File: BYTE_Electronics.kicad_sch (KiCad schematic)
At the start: 9 parts, among them J3 Screw_Terminal_01x04, J4 Screw_Terminal_01x02, J7 Screw_Terminal_01x02, J9 Screw_Terminal_01x02, U1 LM2596S-3.3

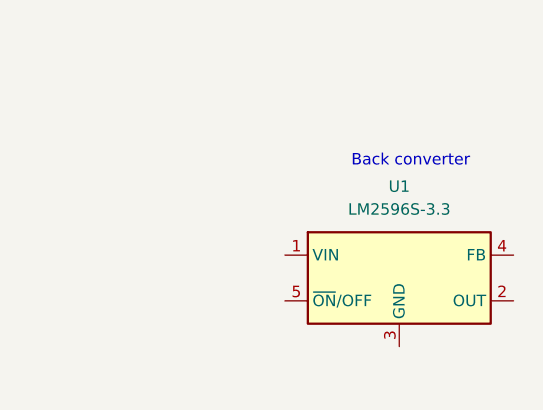
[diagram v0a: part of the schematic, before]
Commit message: Footprint added and minor changes
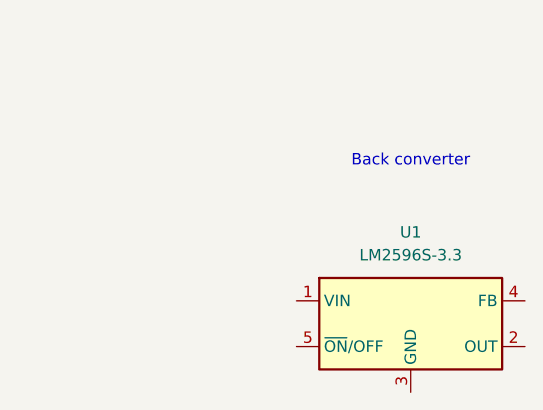
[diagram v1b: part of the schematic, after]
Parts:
- J9: footprint (none) -> Connector_AMASS:AMASS_XT60IPW-M_1x03_P7.20mm_Horizontal; LCSC (none) -> C5334533
- U1: footprint Package_TO_SOT_SMD:TO-263-5_TabPin3 -> Library_mis componentes:BEC_Matek_12S_Pro
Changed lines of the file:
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@@
 			)
 		)
-		(property "Footprint" ""
+		(property "Footprint" "Connector_AMASS:AMASS_XT60IPW-M_1x03_P7.20mm_Horizontal"
 			(at 113.03 27.94 0)
 			(effects
@@
 			)
 		)
+		(property "LCSC" "C5334533"
+			(at 113.03 27.94 0)
+			(effects
+				(font
+					(size 1.27 1.27)
+				)
+				(hide yes)
+			)
+		)
 		(pin "1"
 		)
@@
 				(path "/0c60501e-60f9-4c7f-923a-18a46703e785"
 					(reference "J9")
+					(unit 1)
+				)
+			)
+		)
+	)
+	(symbol
+		(lib_id "Regulator_Switching:LM2596S-3.3")
+		(at 133.35 119.38 0)
+		(unit 1)
+		(exclude_from_sim no)
+		(in_bom yes)
+		(on_board yes)
+		(dnp no)
+		(fields_autoplaced yes)
+		(property "Reference" "U1"
+			(at 133.35 109.22 0)
+			(effects
+				(font
+					(size 1.27 1.27)
+				)
+			)
+		)
+		(property "Value" "LM2596S-3.3"
+			(at 133.35 111.76 0)
+			(effects
+				(font
+					(size 1.27 1.27)
+				)
+			)
+		)
+		(property "Footprint" "Library_mis componentes:BEC_Matek_12S_Pro"
+			(at 134.62 125.73 0)
+			(effects
+				(font
+					(size 1.27 1.27)
+					(italic yes)
+				)
+				(justify left)
+				(hide yes)
+			)
+		)
+		(property "Datasheet" ""
+			(at 133.35 119.38 0)
+			(effects
+				(font
+					(size 1.27 1.27)
+				)
+				(hide yes)
+			)
+		)
+		(property "Description" ""
+			(at 133.35 119.38 0)
+			(effects
+				(font
+					(size 1.27 1.27)
+				)
+				(hide yes)
+			)
+		)
+		(pin "4"
+		)
+		(pin "1"
+		)
+		(pin "3"
+		)
+		(pin "2"
+		)
+		(pin "5"
+		)
+		(instances
+			(project ""
+				(path "/0c60501e-60f9-4c7f-923a-18a46703e785"
+					(reference "U1")
 					(unit 1)
 				)
@@
 			)
 		)
+		(property "LCSC" ""
+			(at 52.07 113.03 0)
+			(effects
+				(font
+					(size 1.27 1.27)
+				)
+				(hide yes)
+			)
+		)
 		(pin "1"
 		)
@@
 			)
 		)
+		(property "LCSC" ""
+			(at 113.03 46.99 0)
+			(effects
+				(font
+					(size 1.27 1.27)
+				)
+				(hide yes)
+			)
+		)
 		(pin "1"
 		)
@@
 			)
 		)
+		(property "LCSC" ""
+			(at 113.03 64.77 0)
+			(effects
+				(font
+					(size 1.27 1.27)
+				)
+				(hide yes)
+			)
+		)
 		(pin "1"
 		)
@@
 			)
 		)
+		(property "LCSC" ""
+			(at 52.07 101.6 0)
+			(effects
+				(font
+					(size 1.27 1.27)
+				)
+				(hide yes)
+			)
+		)
 		(pin "1"
 		)
@@
 			)
 		)
+		(property "LCSC" ""
+			(at 46.99 43.18 0)
+			(effects
+				(font
+					(size 1.27 1.27)
+				)
+				(hide yes)
+			)
+		)
 		(pin "1"
 		)
@@
 				(path "/0c60501e-60f9-4c7f-923a-18a46703e785"
 					(reference "J3")
-					(unit 1)
-				)
-			)
-		)
-	)
-	(symbol
-		(lib_id "Regulator_Switching:LM2596S-3.3")
-		(at 132.08 114.3 0)
-		(unit 1)
-		(exclude_from_sim no)
-		(in_bom yes)
-		(on_board yes)
-		(dnp no)
-		(fields_autoplaced yes)
-		(property "Reference" "U1"
-			(at 132.08 104.14 0)
-			(effects
-				(font
-					(size 1.27 1.27)
-				)
-			)
-		)
-		(property "Value" "LM2596S-3.3"
-			(at 132.08 106.68 0)
-			(effects
-				(font
-					(size 1.27 1.27)
-				)
-			)
-		)
-		(property "Footprint" "Package_TO_SOT_SMD:TO-263-5_TabPin3"
-			(at 133.35 120.65 0)
-			(effects
-				(font
-					(size 1.27 1.27)
-					(italic yes)
-				)
-				(justify left)
-				(hide yes)
-			)
-		)
-		(property "Datasheet" "http://www.ti.com/lit/ds/symlink/lm2596.pdf"
-			(at 132.08 114.3 0)
-			(effects
-				(font
-					(size 1.27 1.27)
-				)
-				(hide yes)
-			)
-		)
-		(property "Description" "3.3V 3A Step-Down Voltage Regulator, TO-263"
-			(at 132.08 114.3 0)
-			(effects
-				(font
-					(size 1.27 1.27)
-				)
-				(hide yes)
-			)
-		)
-		(pin "1"
-		)
-		(pin "2"
-		)
-		(pin "5"
-		)
-		(pin "3"
-		)
-		(pin "4"
-		)
-		(instances
-			(project "BYTE_Electronics"
-				(path "/0c60501e-60f9-4c7f-923a-18a46703e785"
-					(reference "U1")
 					(unit 1)
 				)
@@
 			)
 		)
+		(property "LCSC" ""
+			(at 72.39 113.03 0)
+			(effects
+				(font
+					(size 1.27 1.27)
+				)
+				(hide yes)
+			)
+		)
 		(pin "1"
 		)
@@
 			(at 72.39 101.6 0)
 			(effects
+				(font
+					(size 1.27 1.27)
+				)
+				(hide yes)
+			)
+		)
+		(property "LCSC" ""
+			(at 72.39 101.6 0)
+			(effects

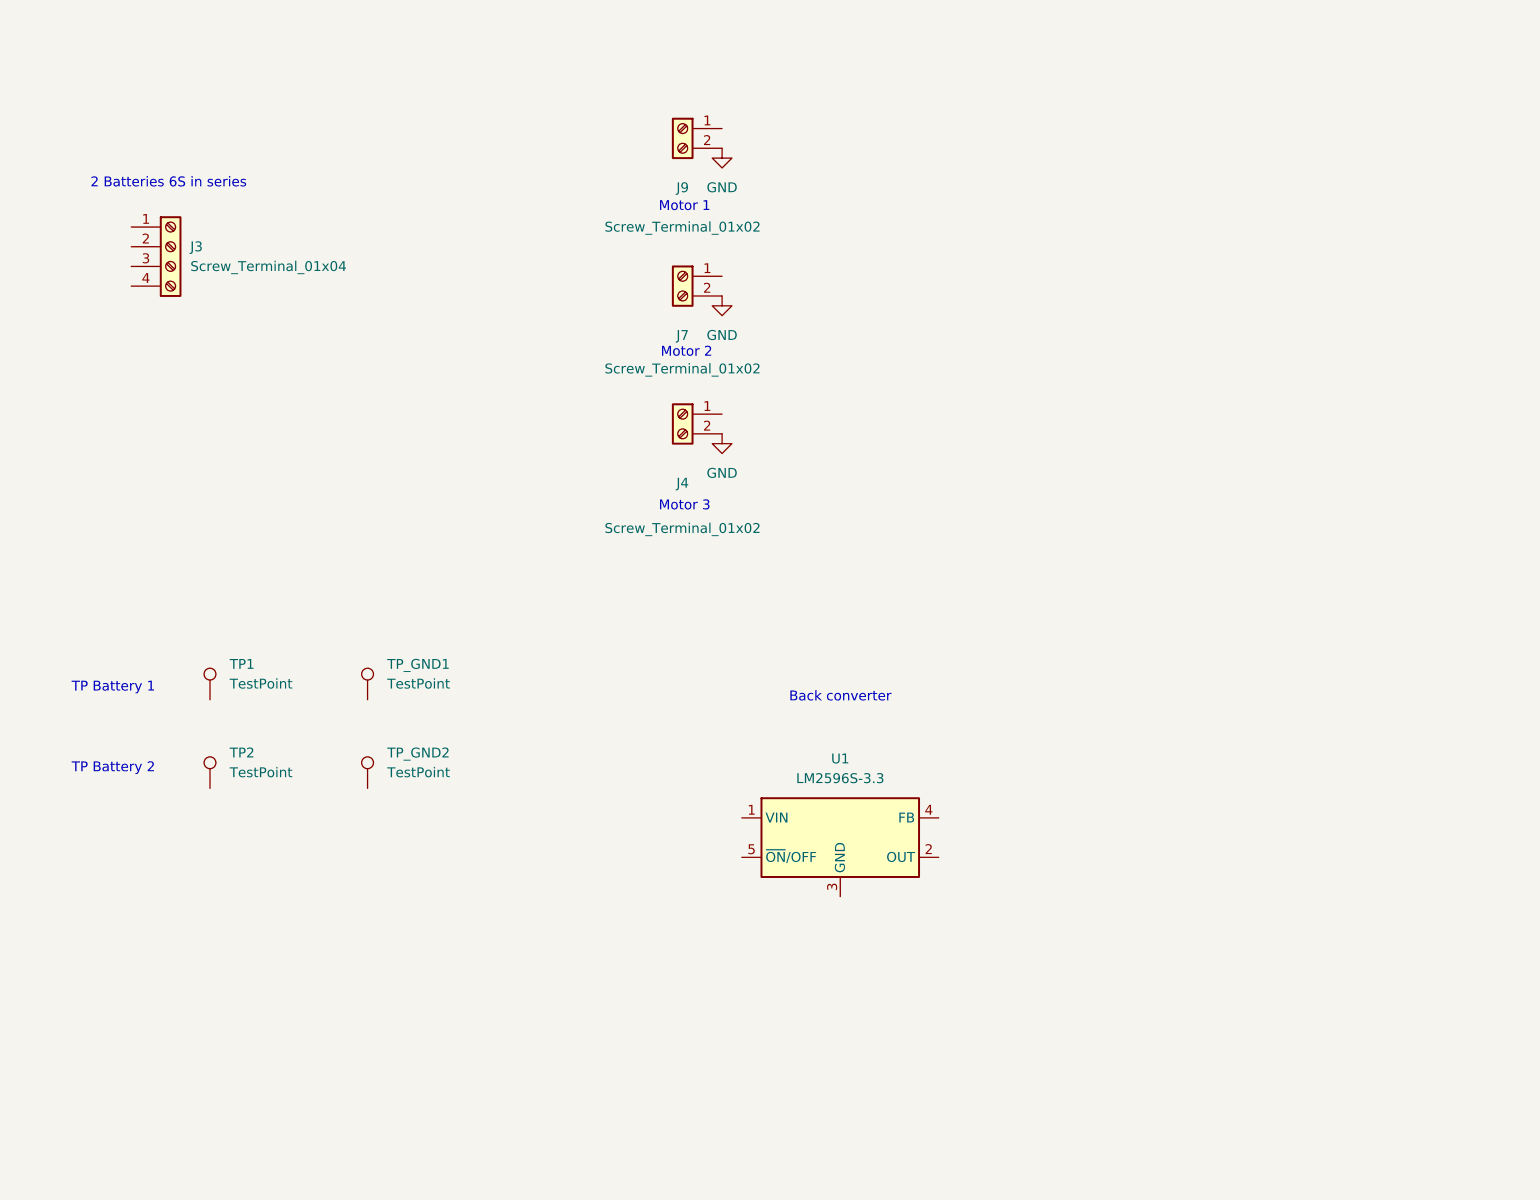
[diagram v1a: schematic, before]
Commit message: Avencement du pcb avec connexions
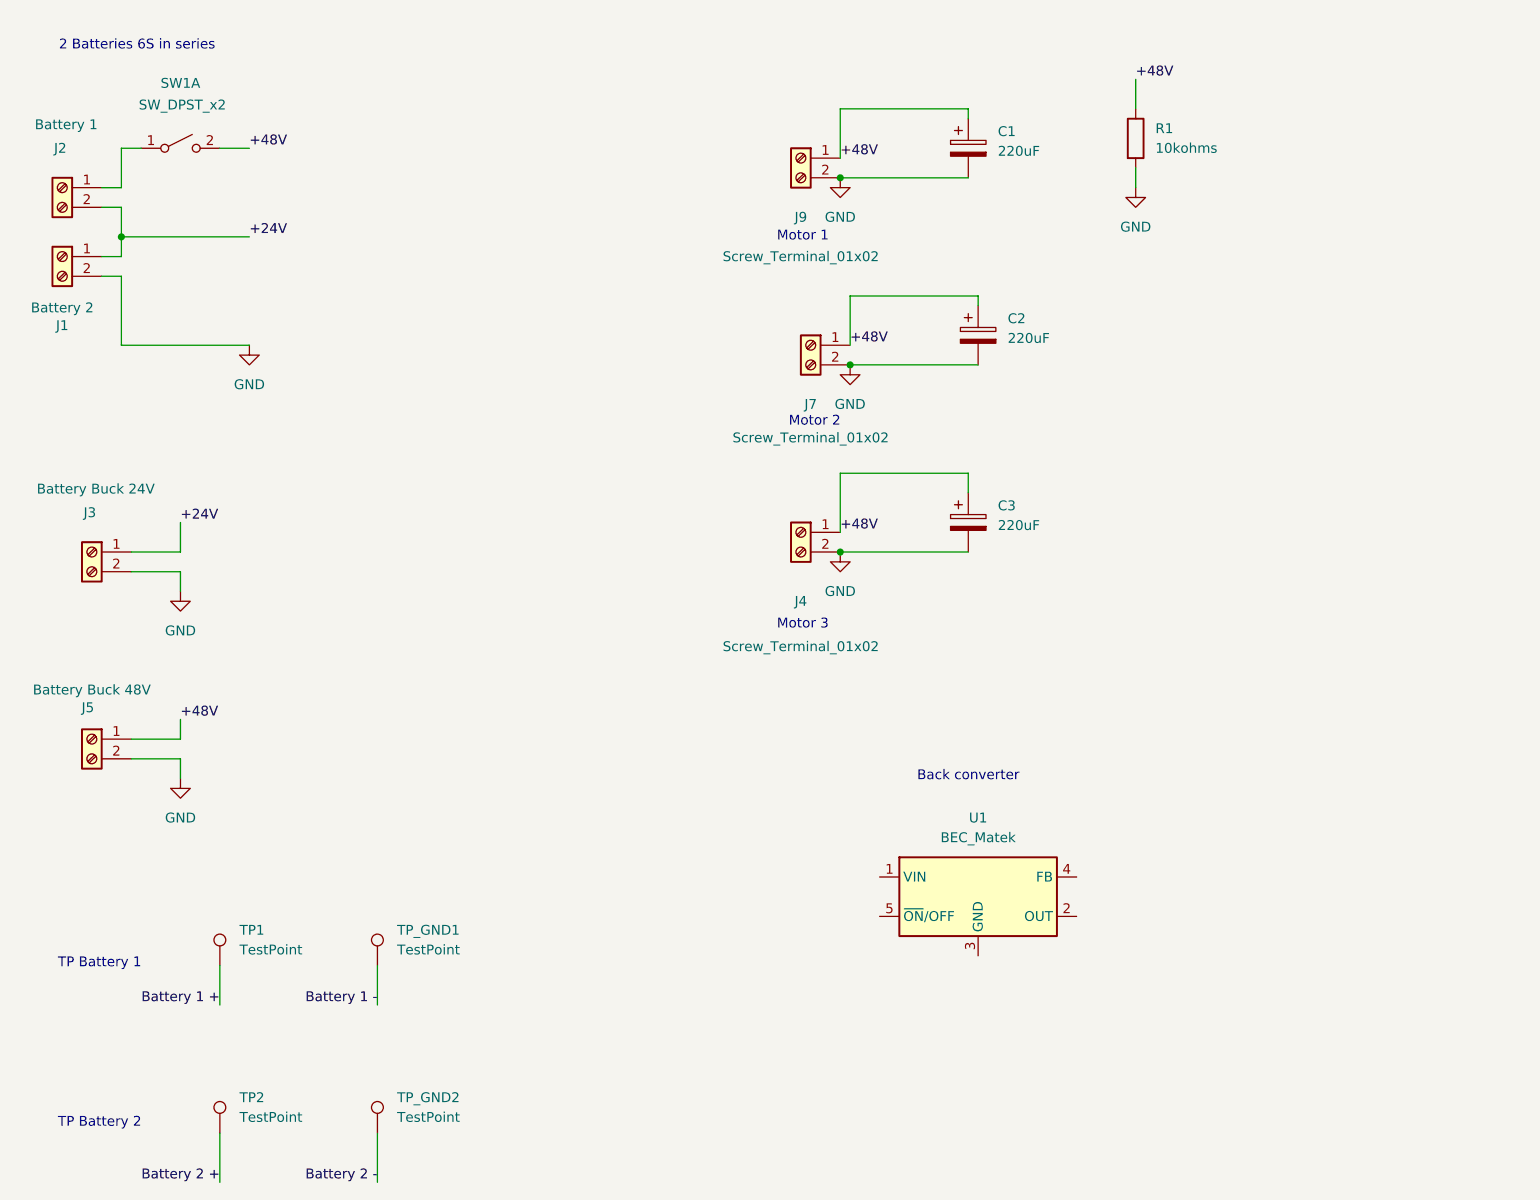
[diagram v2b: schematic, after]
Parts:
- removed J3: Screw_Terminal_01x04, symbol Connector:Screw_Terminal_01x04
- added C1, C2, C3: 220uF, symbol Device:C_Polarized
- added J1: Battery 2, symbol Connector:Screw_Terminal_01x02
- added J2: Battery 1, symbol Connector:Screw_Terminal_01x02
- added J3: Battery Buck 24V, symbol Connector:Screw_Terminal_01x02
- added J5: Battery Buck 48V, symbol Connector:Screw_Terminal_01x02
- added R1: 10kohms, symbol Device:R
- added SW1: SW_DPST_x2, symbol Switch:SW_DPST_x2
- U1: value LM2596S-3.3 -> BEC_Matek
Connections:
- net GND: now also C1.2, C2.2, C3.2, J1.2 (Pin_2), J3.2 (Pin_2), J5.2 (Pin_2), R1.2
- net +48V: now reaches J9.1 (Pin_1)
- net +48V: now also J4.1 (Pin_1), J7.1 (Pin_1), C1.1, C2.1, C3.1, J5.1 (Pin_1), R1.1, SW1.2 (B)
- net Battery 2 +: now reaches TP2.1
- net Battery 1 +: now reaches TP1.1
- net Battery 2 -: now reaches TP_GND2.1
- net Battery 1 -: now reaches TP_GND1.1
- new net: J2.1 (Pin_1), SW1.1 (A)
- new net +24V: J1.1 (Pin_1), J2.2 (Pin_2), J3.1 (Pin_1)
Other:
- moved on the sheet: J4, J7, J9, TP1, TP2, TP_GND1, TP_GND2, U1

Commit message: added footprint to compo exept switch and Buck
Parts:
- C1, C2, C3: value 220uF -> 330uF; footprint (none) -> Footprint_PB_Byte:VZH331M2ATR-1816
- J1, J2: footprint (none) -> Connector_AMASS:AMASS_XT90PW-M_1x02_P10.90mm_Horizontal
- J4, J7: footprint (none) -> Connector_AMASS:AMASS_XT30PW-M_1x02_P2.50mm_Horizontal
- J9: footprint Connector_AMASS:AMASS_XT60IPW-M_1x03_P7.20mm_Horizontal -> Connector_AMASS:AMASS_XT30PW-M_1x02_P2.50mm_Horizontal; LCSC C5334533 -> (none)
- R1: value 10kohms -> 100kohms; footprint (none) -> Resistor_SMD:R_2512_6332Metric_Pad1.40x3.35mm_HandSolder; LCSC (none) -> C25717
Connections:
- no-connect marks 0 -> 1
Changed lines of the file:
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@@
 		(color 0 0 0 0)
 	)
+	(no_connect
+		(at 220.98 13.97)
+	)
 	(wire
 		(pts
@@
 	(wire
 		(pts
+			(xy 171.45 21.59) (xy 171.45 25.4)
+		)
+		(stroke
+			(width 0)
+			(type default)
+		)
+	)
+	(wire
+		(pts
 			(xy 53.34 157.48) (xy 53.34 163.83)
 		)
@@
 		(pts
 			(xy 38.1 38.1) (xy 40.64 38.1)
-		)
-		(stroke
-			(width 0)
-			(type default)
-		)
-	)
-	(wire
-		(pts
-			(xy 171.45 21.59) (xy 171.45 25.4)
 		)
 		(stroke
@@
 			)
 		)
-		(property "Footprint" ""
+		(property "Footprint" "Connector_AMASS:AMASS_XT90PW-M_1x02_P10.90mm_Horizontal"
 			(at 33.02 44.45 0)
 			(effects
@@
 			)
 		)
-		(property "Footprint" "Connector_AMASS:AMASS_XT60IPW-M_1x03_P7.20mm_Horizontal"
+		(property "Footprint" "Connector_AMASS:AMASS_XT30PW-M_1x02_P2.50mm_Horizontal"
 			(at 128.27 31.75 0)
 			(effects
@@
 			)
 		)
-		(property "LCSC" "C5334533"
+		(property "LCSC" ""
 			(at 128.27 31.75 0)
 			(effects
@@
 			)
 		)
-		(property "Value" "10kohms"
+		(property "Value" "100kohms"
 			(at 173.99 30.4799 0)
 			(effects
@@
 			)
 		)
-		(property "Footprint" ""
+		(property "Footprint" "Resistor_SMD:R_2512_6332Metric_Pad1.40x3.35mm_HandSolder"
 			(at 169.672 29.21 90)
 			(effects
@@
 		)
 		(property "Description" "Resistor"
+			(at 171.45 29.21 0)
+			(effects
+				(font
+					(size 1.27 1.27)
+				)
+				(hide yes)
+			)
+		)
+		(property "LCSC" "C25717"
 			(at 171.45 29.21 0)
 			(effects
@@
 			)
 		)
-		(property "Footprint" ""
+		(property "Footprint" "Connector_AMASS:AMASS_XT30PW-M_1x02_P2.50mm_Horizontal"
 			(at 129.54 55.88 0)
 			(effects
@@
 			)
 		)
-		(property "Footprint" ""
+		(property "Footprint" "Connector_AMASS:AMASS_XT30PW-M_1x02_P2.50mm_Horizontal"
 			(at 128.27 80.01 0)
 			(effects
@@
 			)
 		)
-		(property "Value" "220uF"
+		(property "Value" "330uF"
 			(at 154.94 54.9909 0)
 			(effects
@@
 			)
 		)
-		(property "Footprint" ""
+		(property "Footprint" "Footprint_PB_Byte:VZH331M2ATR-1816"
 			(at 152.0952 58.42 0)
 			(effects
@@
 			)
 		)
-		(property "Datasheet" "~"
+		(property "Datasheet" "https://jlcpcb.com/partdetail/Lelon-VZH331M2ATR1816/C176687"
 			(at 151.13 54.61 0)
 			(effects
@@
 			)
 		)
-		(property "Footprint" ""
+		(property "Footprint" "Connector_AMASS:AMASS_XT90PW-M_1x02_P10.90mm_Horizontal"
 			(at 33.02 35.56 0)
 			(effects
@@
 			)
 		)
-		(property "Value" "220uF"
+		(property "Value" "330uF"
 			(at 153.67 30.8609 0)
 			(effects
@@
 			)
 		)
-		(property "Footprint" ""
+		(property "Footprint" "Footprint_PB_Byte:VZH331M2ATR-1816"
 			(at 150.8252 34.29 0)
 			(effects
@@
 			)
 		)
-		(property "Value" "220uF"
+		(property "Value" "330uF"
 			(at 153.67 79.1209 0)
 			(effects
@@
 			)
 		)
-		(property "Footprint" ""
+		(property "Footprint" "Footprint_PB_Byte:VZH331M2ATR-1816"
 			(at 150.8252 82.55 0)
 			(effects
@@
 			(at 149.86 78.74 0)
 			(effects
+				(font
+					(size 1.27 1.27)
+				)
+				(hide yes)
+			)
+		)
+		(property "Field5" ""
+			(at 149.86 78.74 0)
+			(effects
